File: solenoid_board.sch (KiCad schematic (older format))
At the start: 34 parts, among them J1 MCU_LEFT_LEGS, J3 MCU_RIGHT_LEGS

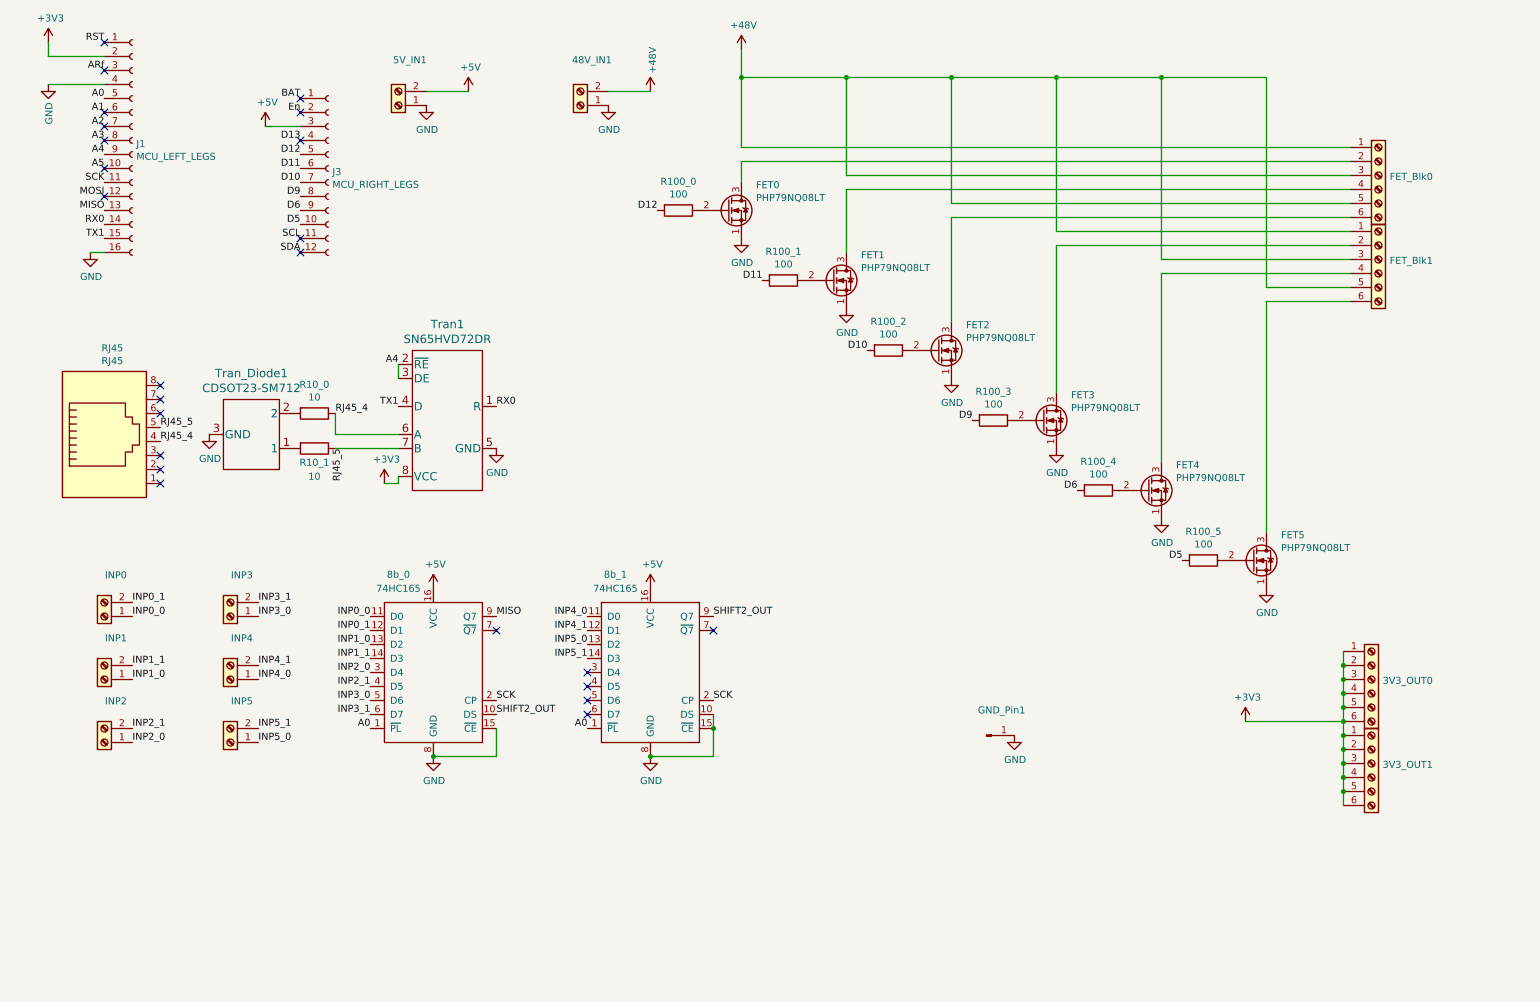
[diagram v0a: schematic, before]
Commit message: Reset PCB after design discussion. New plan is to add a 01x06 screw terminal/3v3 rail output, a 01x02 screw terminal for +5V source, a large capacitor on the supply of the MCU, and a small capacitor on the supply of the 8-bit shift registers & the RS-485 Transciever. The PCB layout will then be slightly changed (but not much) and the whole project organized in such a way as to allow for easy ordering from the Chinese industrial complex.
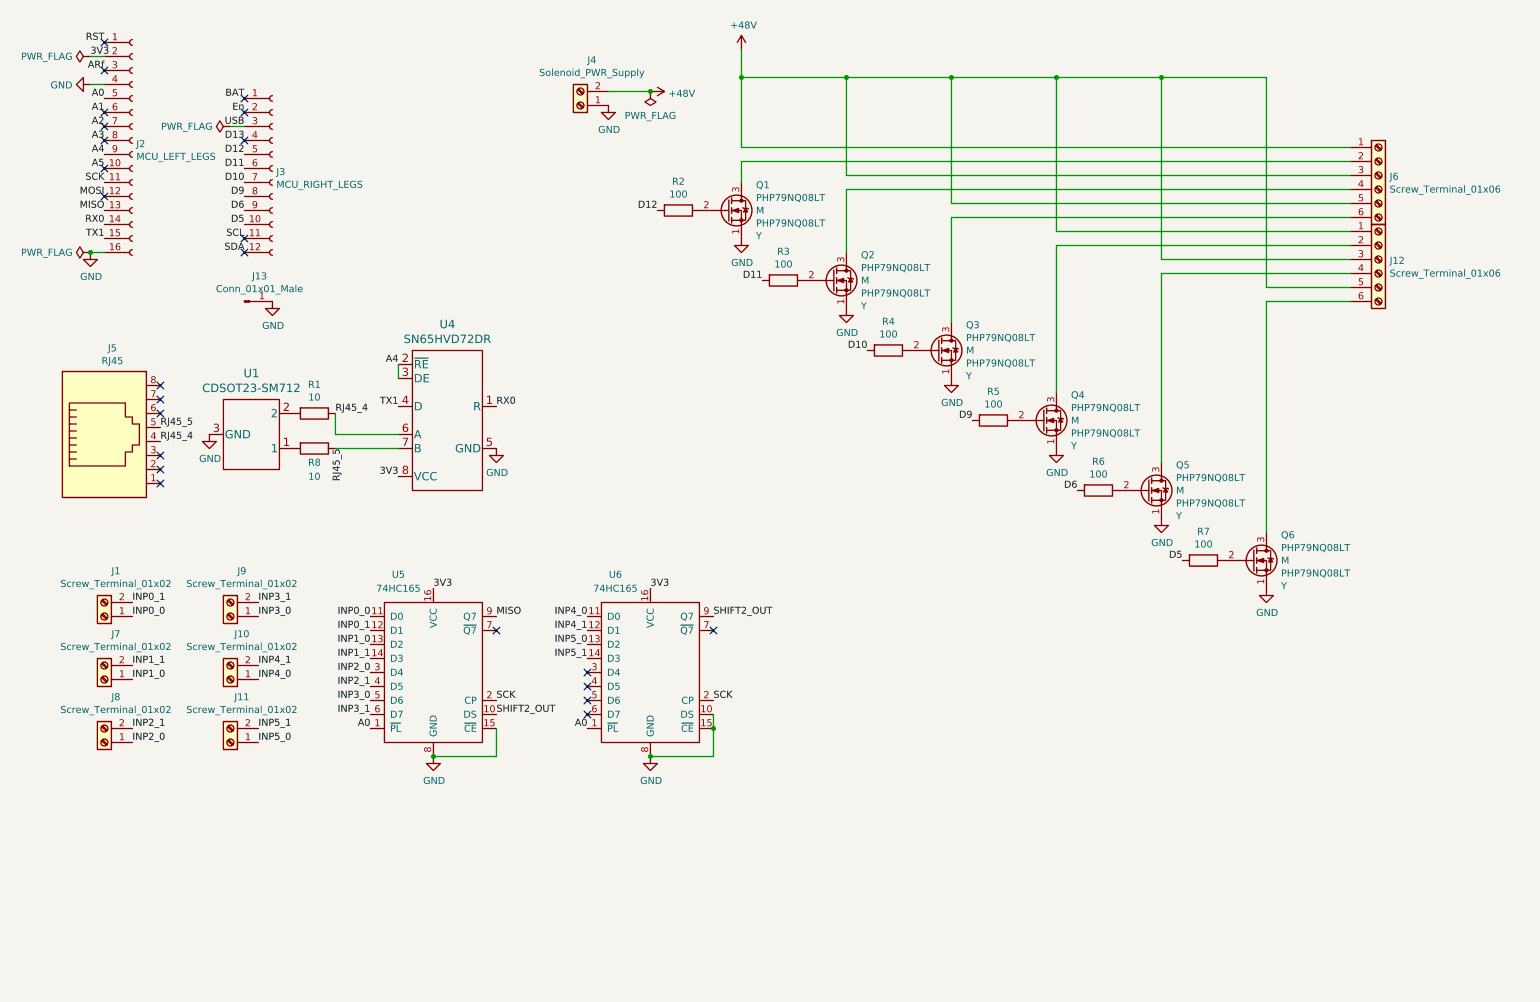
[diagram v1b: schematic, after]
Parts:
- removed 3V3_OUT0, 3V3_OUT1: Screw_Terminal_01x06, TerminalBlock:TerminalBlock_bornier-6_P5.08mm, symbol Connector:Screw_Terminal_01x06
- removed 5V_IN1: Screw_Terminal_01x02, TerminalBlock:TerminalBlock_bornier-2_P5.08mm, symbol Connector:Screw_Terminal_01x02
- J13: renamed from GND_Pin1; value GND -> Conn_01x01_Male
- J4: renamed from 48V_IN1; value Screw_Terminal_01x02 -> Solenoid_PWR_Supply
- renumbered INP0 to J1, INP4 to J10, INP5 to J11, FET_Blk1 to J12, J1 to J2, RJ45 to J5, FET_Blk0 to J6, INP1 to J7, INP2 to J8, INP3 to J9, FET0 to Q1, FET1 to Q2, FET2 to Q3, FET3 to Q4, FET4 to Q5, FET5 to Q6, R10_0 to R1, R100_0 to R2, R100_1 to R3, R100_2 to R4, R100_3 to R5, R100_4 to R6, R100_5 to R7, R10_1 to R8, Tran_Diode1 to U1, Tran1 to U4, 8b_0 to U5, 8b_1 to U6
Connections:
- net +3V3 renamed 3V3
- net 3V3: now also U5.16 (VCC), U6.16 (VCC)
- removed net +5V: J3.3 (Pin_3), U5.16 (VCC), U6.16 (VCC)
- new net USB: J3.3 (Pin_3)
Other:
- moved on the sheet: J13, J3

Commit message: Added a +5V Supply input and connected it to the Feather board. Added a second RJ45 port, and connected the 4th and 5th wires of both RJ45 ports together. Added 4 capacitors to maintain a voltage on the supply pins of the digital electronics, and picked out the footprints. Added a +3V3 terminal block, to power the solenoid switches. Changed the supply voltage to the 8-bit shifters from +3V3 to +5V, as is typical according to the datasheet. Still need to clean up the schematic, add a BOM, change the footprint of the large electrolytic capacitor to a smaller size, finalize the geometry of the PCB layout, generate the gerber files, and order the sucker.
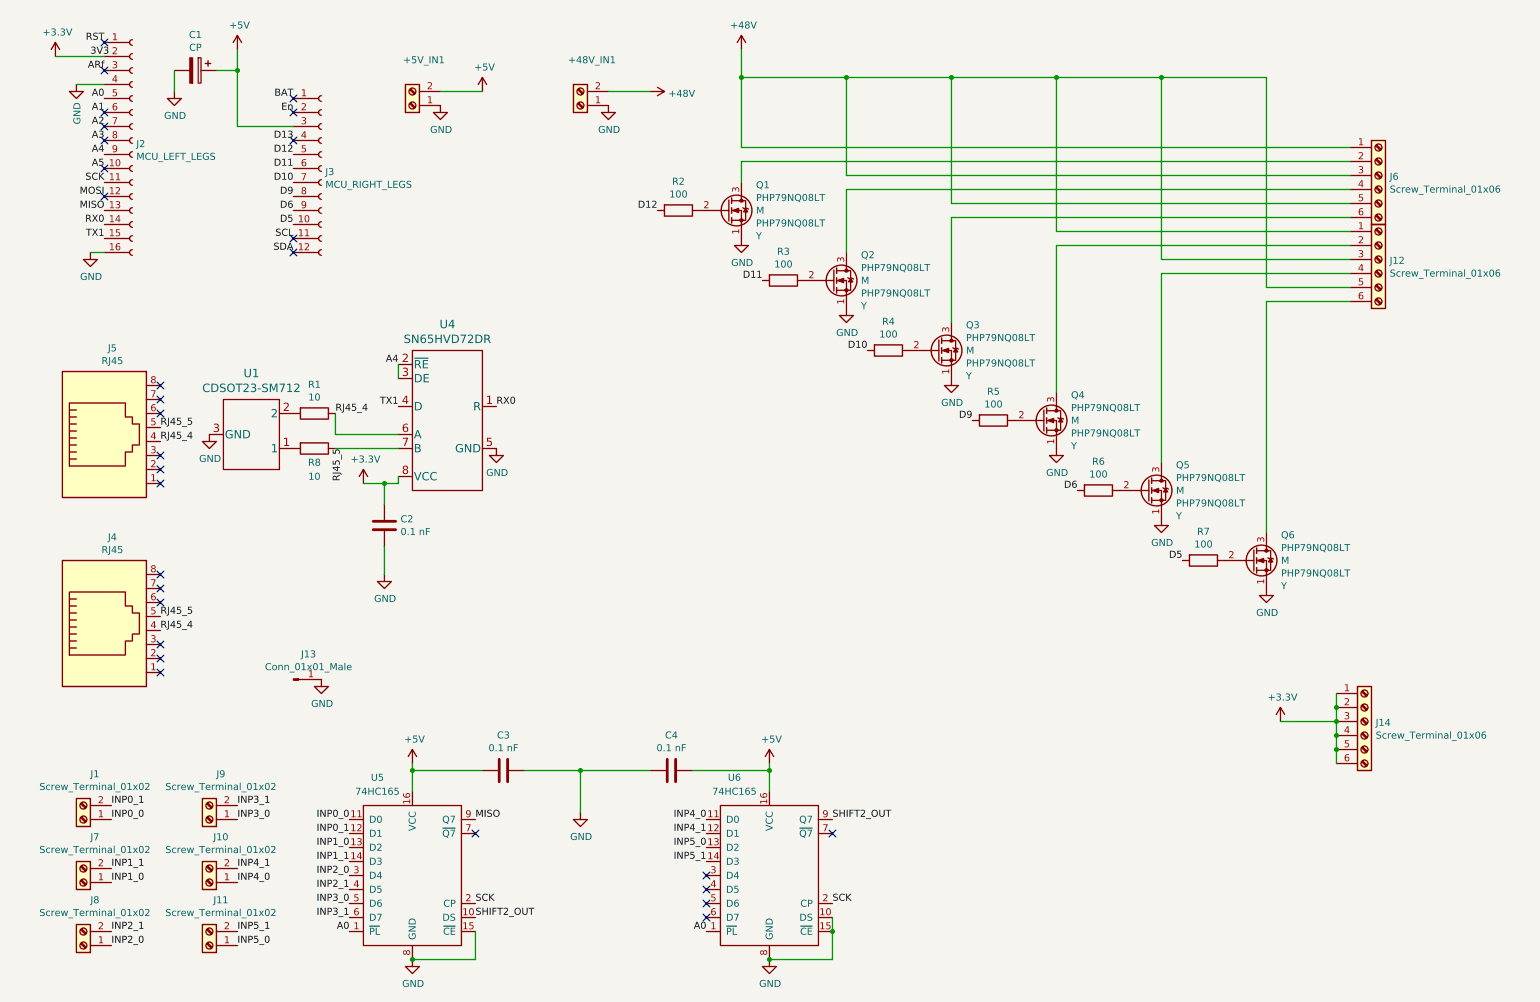
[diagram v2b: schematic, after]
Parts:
- added +5V_IN1: MCU_PWR_Supply, TerminalBlock:TerminalBlock_bornier-2_P5.08mm, symbol Connector:Screw_Terminal_01x02
- added C1: CP, Capacitor_THT:CP_Radial_D8.0mm_P5.00mm, symbol Device:CP
- added C2, C3, C4: 0.1 nF, Capacitor_THT:CP_Radial_D4.0mm_P2.00mm, symbol Device:C
- added J14: Screw_Terminal_01x06, TerminalBlock:TerminalBlock_bornier-6_P5.08mm, symbol Connector:Screw_Terminal_01x06
- added J4: RJ45, Connector_RJ:RJ45_Pulse_JK0654219NL_Horizontal, symbol Connector:RJ45
- renumbered J4 to +48V_IN1
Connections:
- net GND: now also +5V_IN1.1 (Pin_1), C1.2, C2.1, C3.1, C4.2
- net RJ45_4: now also J4.4
- net RJ45_5: now also J4.5
- net 3V3 renamed +3V3
- net +3V3: now also C2.2, J14.1 (Pin_1), J14.2 (Pin_2), J14.3 (Pin_3), J14.4 (Pin_4), J14.5 (Pin_5), J14.6 (Pin_6); no longer U5.16 (VCC), U6.16 (VCC)
- net USB renamed +5V
- net +5V: now also U5.16 (VCC), U6.16 (VCC), +5V_IN1.2 (Pin_2), C1.1, C3.2, C4.1
- no-connect marks 24 -> 30
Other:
- moved on the sheet: J1, J10, J11, J13, J3, J7, J8, J9, U5, U6

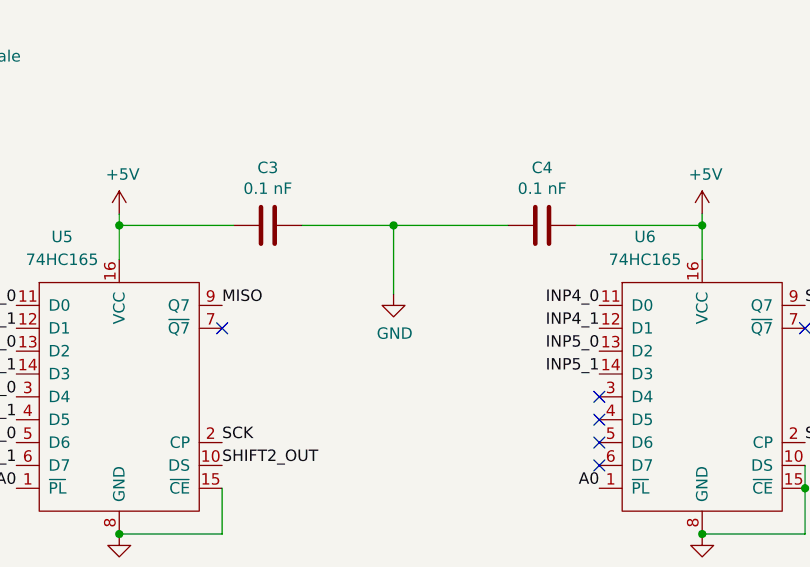
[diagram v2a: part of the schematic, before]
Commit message: Changed the electrolytic capacitor's footprint, deleted all wires in the layout, and rearranged the components.
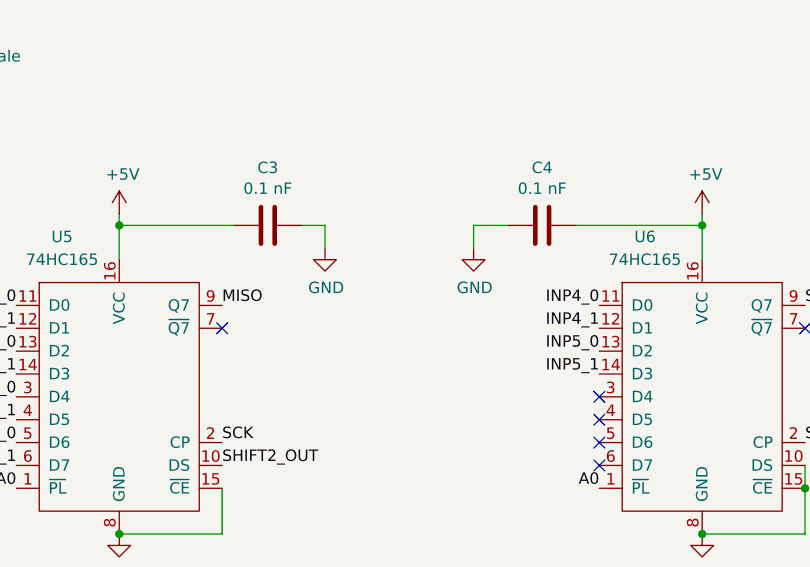
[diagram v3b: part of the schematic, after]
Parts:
- C1: footprint Capacitor_THT:CP_Radial_D8.0mm_P5.00mm -> Capacitor_THT:CP_Radial_D5.0mm_P2.50mm
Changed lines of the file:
@@
 $EndComp
-Wire Wire Line
-	4200 5900 4600 5900
 Wire Wire Line
 	5400 5900 5950 5900
@@
 L power:GND #PWR0111
 U 1 1 5E3D3EA3
-P 4600 6200
-F 0 "#PWR0111" H 4600 5950 50  0001 C CNN
-F 1 "GND" H 4605 6027 50  0000 C CNN
-F 2 "" H 4600 6200 50  0001 C CNN
-F 3 "" H 4600 6200 50  0001 C CNN
-	1    4600 6200
+P 4300 6000
+F 0 "#PWR0111" H 4300 5750 50  0001 C CNN
+F 1 "GND" H 4305 5827 50  0000 C CNN
+F 2 "" H 4300 6000 50  0001 C CNN
+F 3 "" H 4300 6000 50  0001 C CNN
+	1    4300 6000
 	1    0    0    -1
 $EndComp
-Wire Wire Line
-	4600 6200 4600 5900
-Connection ~ 4600 5900
-Wire Wire Line
-	4600 5900 5100 5900
 $Comp
 L Device:C C2
@@
 F 0 "C1" V 1595 900 50  0000 C CNN
 F 1 "CP" V 1686 900 50  0000 C CNN
-F 2 "Capacitor_THT:CP_Radial_D8.0mm_P5.00mm" H 1888 750 50  0001 C CNN
+F 2 "Capacitor_THT:CP_Radial_D5.0mm_P2.50mm" H 1888 750 50  0001 C CNN
 F 3 "~" H 1850 900 50  0001 C CNN
 	1    1850 900
@@
 Wire Wire Line
 	9600 5550 10000 5550
+$Comp
+L power:GND #PWR?
+U 1 1 5E34A4C6
+P 4950 6000
+F 0 "#PWR?" H 4950 5750 50  0001 C CNN
+F 1 "GND" H 4955 5827 50  0000 C CNN
+F 2 "" H 4950 6000 50  0001 C CNN
+F 3 "" H 4950 6000 50  0001 C CNN
+	1    4950 6000
+	1    0    0    -1
+$EndComp
+Wire Wire Line
+	4200 5900 4300 5900
+Wire Wire Line
+	4300 5900 4300 6000
+Wire Wire Line
+	5100 5900 4950 5900
+Wire Wire Line
+	4950 5900 4950 6000
 $EndSCHEMATC

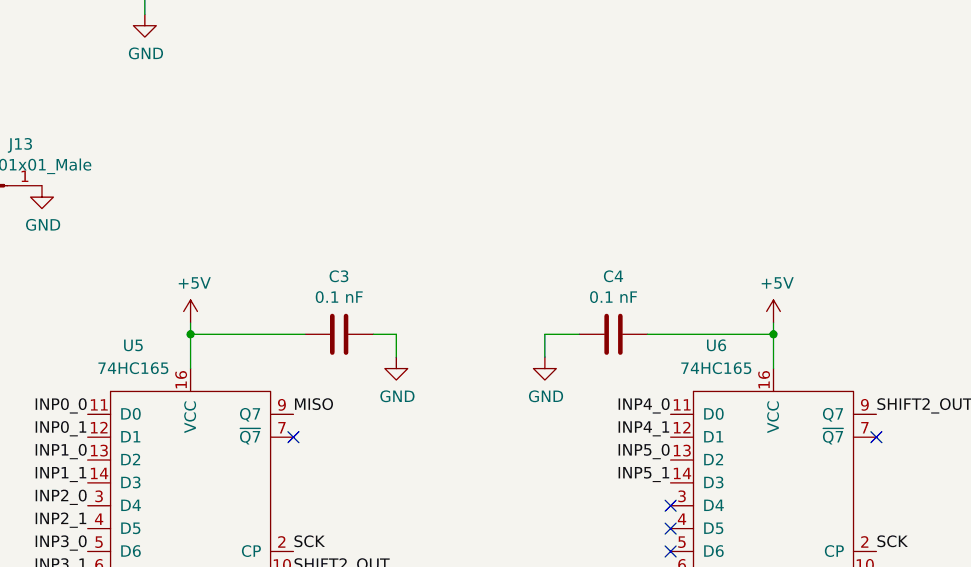
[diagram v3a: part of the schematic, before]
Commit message: Increased board size by half a centimeter on the left side so that the 3.3V terminal strip isn't all up in the feather m0's business. Rearranged the PCB layout geometry a bit. Moved the 8-shift registers back to 3.3V because of the volatility of the +5V signal.
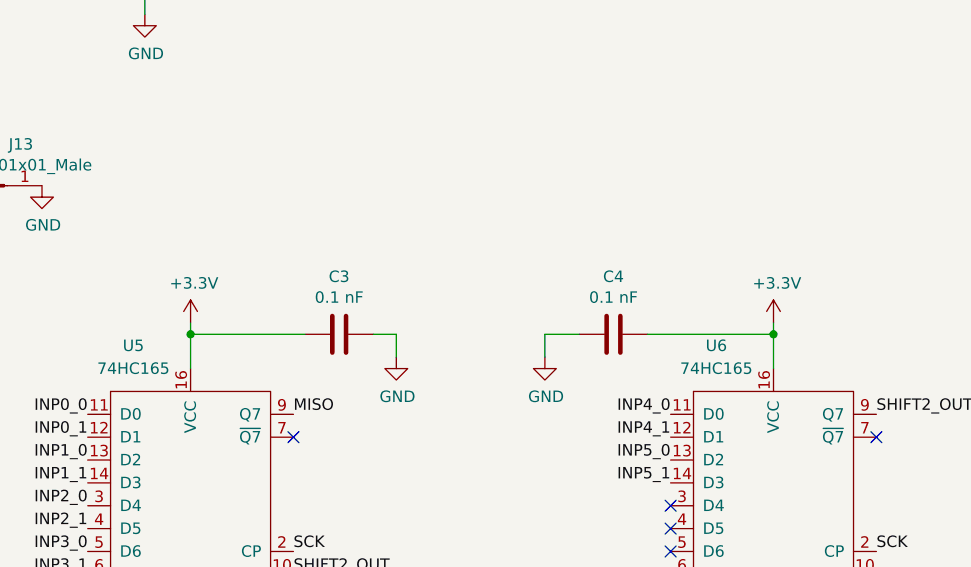
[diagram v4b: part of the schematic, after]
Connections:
- net +3V3: now also C3.2, C4.1, U5.16 (VCC), U6.16 (VCC)
- net +5V: no longer C3.2, C4.1, U5.16 (VCC), U6.16 (VCC)
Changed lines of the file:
@@
-	1    0    0    -1
-$EndComp
-$Comp
-L power:+5V #PWR0108
-U 1 1 5E39414D
-P 3400 5850
-F 0 "#PWR0108" H 3400 5700 50  0001 C CNN
-F 1 "+5V" H 3415 6023 50  0000 C CNN
-F 2 "" H 3400 5850 50  0001 C CNN
-F 3 "" H 3400 5850 50  0001 C CNN
-	1    3400 5850
-	1    0    0    -1
-$EndComp
-$Comp
-L power:+5V #PWR0109
-U 1 1 5E39B230
-P 5950 5850
-F 0 "#PWR0109" H 5950 5700 50  0001 C CNN
-F 1 "+5V" H 5965 6023 50  0000 C CNN
-F 2 "" H 5950 5850 50  0001 C CNN
-F 3 "" H 5950 5850 50  0001 C CNN
-	1    5950 5850
 	1    0    0    -1
 $EndComp
@@
 	9600 5550 10000 5550
 $Comp
-L power:GND #PWR?
+L power:GND #PWR0115
 U 1 1 5E34A4C6
 P 4950 6000
-F 0 "#PWR?" H 4950 5750 50  0001 C CNN
+F 0 "#PWR0115" H 4950 5750 50  0001 C CNN
 F 1 "GND" H 4955 5827 50  0000 C CNN
 F 2 "" H 4950 6000 50  0001 C CNN
@@
 Wire Wire Line
 	4950 5900 4950 6000
+$Comp
+L power:+3.3V #PWR?
+U 1 1 5E365E3D
+P 3400 5850
+F 0 "#PWR?" H 3400 5700 50  0001 C CNN
+F 1 "+3.3V" H 3415 6023 50  0000 C CNN
+F 2 "" H 3400 5850 50  0001 C CNN
+F 3 "" H 3400 5850 50  0001 C CNN
+	1    3400 5850
+	1    0    0    -1
+$EndComp
+$Comp
+L power:+3.3V #PWR?
+U 1 1 5E366586
+P 5950 5850
+F 0 "#PWR?" H 5950 5700 50  0001 C CNN
+F 1 "+3.3V" H 5965 6023 50  0000 C CNN
+F 2 "" H 5950 5850 50  0001 C CNN
+F 3 "" H 5950 5850 50  0001 C CNN
+	1    5950 5850
+	1    0    0    -1
+$EndComp
 $EndSCHEMATC
